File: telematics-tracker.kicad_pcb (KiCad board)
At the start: 4 copper layers, 82 x 62 mm, 216 parts, among them J1 WAFER-MX3.0-12PZZ, J2 B3B-XH-A, Q1 AM2390N-TP, Q10 MMBT3904, Q11 MMBT3904, Q12 MMBT3904, Q13 MMBT3906, Q14 MMBT3904, Q2 AM2390N-TP, Q3 AO3401A, Q4 MMBT3904, Q5 MMBT3904, Q6 MMBT3904, Q7 MMBT3904, Q8 MMBT3904, Q9 MMBT3904, U1 EC200UCNAA-N05-SGNSA, U2 AT32F403ACGT7, U3 QMI8658B, U4 SIT1051AT/3, U5 EG11752, U6 BQ25606RGER, U7 GD25Q64ESIGR, U8 TXB0104PWR, U9 ME6211C33M5G, X1 NANO-SIM, X2 MFF2-eSIM-pads, Y1 8MHz, Y2 32.768kHz

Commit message: hybrid v11 cycle 1: unconnected=150 errors=0
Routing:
- net 3V3: track 24.0 -> 54.1 mm
- net /modem_rf/VDD_EXT_1V8: track 86.2 -> 89.1 mm
- net 5V0: track 292.8 -> 294.7 mm, vias 22 -> 13
- net /mcu/BOOT0: track 2.42 -> 3.99 mm
- net /io/CAN_SPLIT: track 51.6 -> 53.1 mm
- net /mcu/VBAT_MCU: track 30.1 -> 31.5 mm
- net /modem_rf/Q12_B: track 120.4 -> 121.5 mm
- net /modem_rf/USIM_RST_M: track 77.6 -> 78.7 mm
- net /mcu/OSC32_IN: track 17.2 -> 18.3 mm
- net /mcu/I2C1_SDA: track 14.4 -> 15.1 mm
- net /mcu/I2C1_SCL: track 15.0 -> 15.7 mm
- net MODEM_PWRKEY: track 67.4 -> 68.0 mm

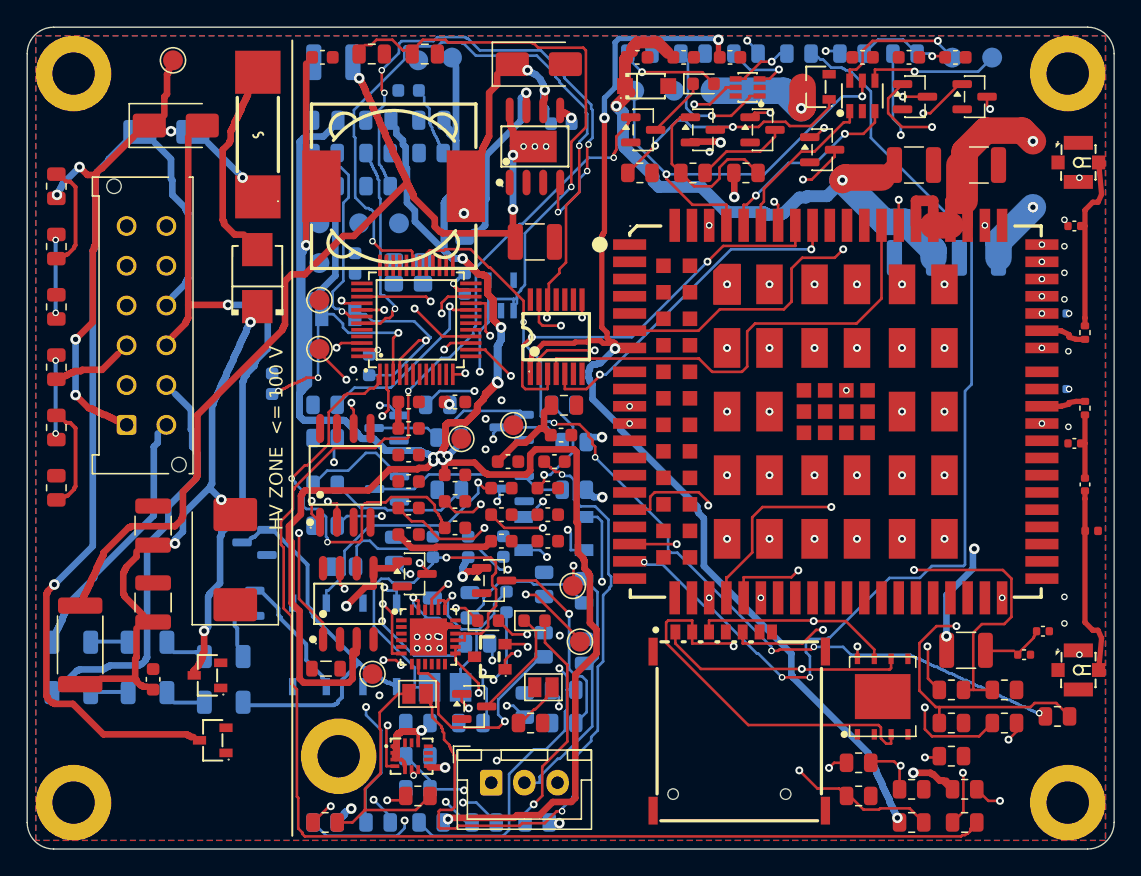
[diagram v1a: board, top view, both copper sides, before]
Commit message: hybrid v12 cycle 1: unconnected=110 errors=0
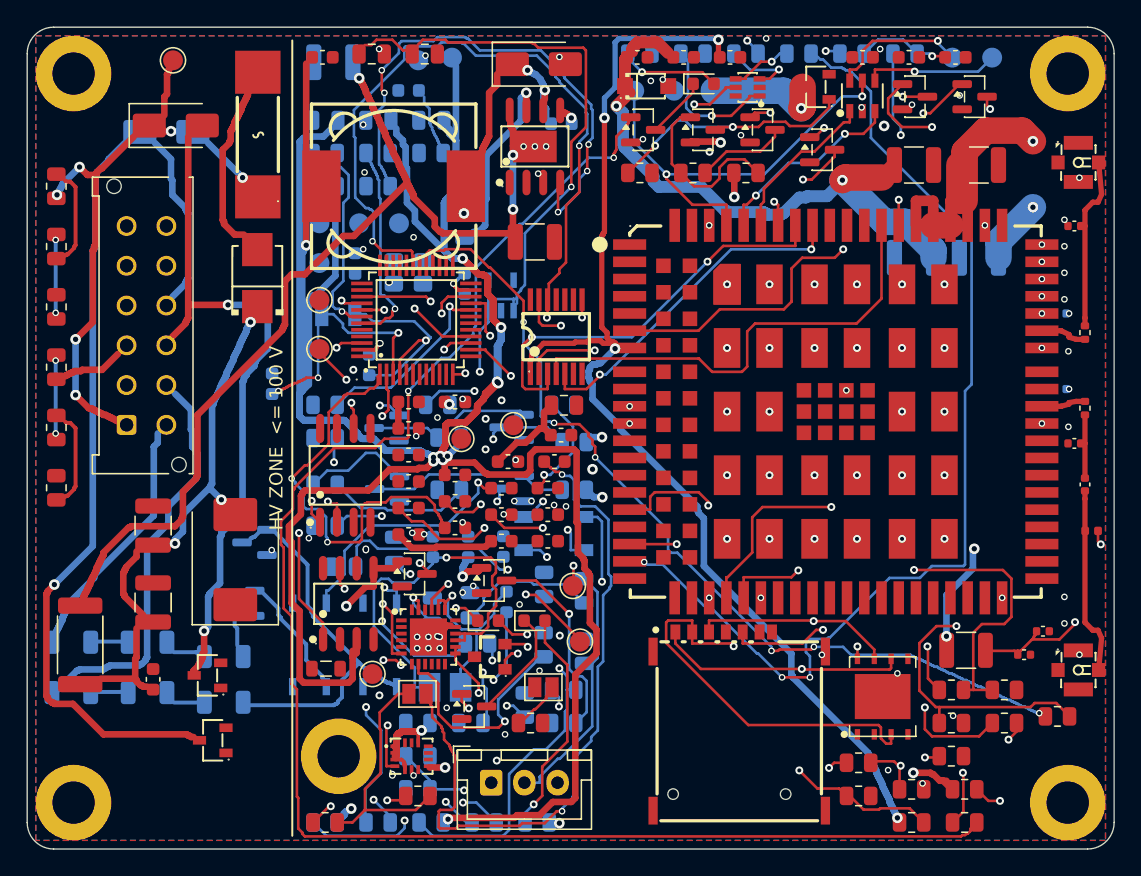
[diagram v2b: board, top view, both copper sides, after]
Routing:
- net /modem_rf/GNSS_BIAS: track 3.36 -> 16.6 mm, vias 0 -> 2
- net GND: track 3.62 -> 3.75 mm, vias 63 -> 112
- net 5V0: vias 13 -> 14
- net /modem_rf/VBAT_MODEM: vias 5 -> 6

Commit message: hybrid v12 cycle 2: unconnected=110 errors=0
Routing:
- net GND: vias 112 -> 110
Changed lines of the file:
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@@
 	(segment
 		(start 33.8996 45.4275)
-		(end 32.7628 45.4275)
+		(end 33.8996 47.2187)
 		(width 0.2)
 		(layer "B.Cu")
@@
 	(segment
 		(start 33.8996 45.4275)
-		(end 33.8996 47.2187)
+		(end 32.7628 45.4275)
 		(width 0.2)
 		(layer "B.Cu")
@@
 	(segment
 		(start 35.55 23.95)
-		(end 35.45 24.05)
+		(end 35.55 26.85)
 		(width 0.5)
 		(layer "B.Cu")
@@
 	(segment
 		(start 35.55 23.95)
-		(end 35.55 26.85)
+		(end 35.45 24.05)
 		(width 0.5)
 		(layer "B.Cu")
@@
 	(segment
 		(start 26.13 40.82)
-		(end 27.7625 40.82)
+		(end 26.13 42.2042)
 		(width 0.5)
 		(layer "F.Cu")
@@
 	(segment
 		(start 26.13 40.82)
-		(end 26.13 42.2042)
+		(end 27.7625 40.82)
 		(width 0.5)
 		(layer "F.Cu")
@@
 	(segment
 		(start 27.85 53.55)
-		(end 27.95 53.45)
+		(end 27.85 53.45)
 		(width 0.5)
 		(layer "F.Cu")
@@
 	(segment
 		(start 27.85 53.55)
-		(end 27.85 53.45)
+		(end 27.95 53.45)
 		(width 0.5)
 		(layer "F.Cu")
@@
 	(segment
 		(start 27.85 54.4)
-		(end 27.85 54.15)
+		(end 27.74 54.29)
 		(width 0.5)
 		(layer "F.Cu")
@@
 	(segment
 		(start 27.85 54.4)
-		(end 27.74 54.29)
+		(end 27.85 54.15)
 		(width 0.5)
 		(layer "F.Cu")
@@
 	(segment
 		(start 29.445 53.15)
-		(end 29.65 53.15)
+		(end 29.5 53.205)
 		(width 0.5)
 		(layer "F.Cu")
@@
 	(segment
 		(start 29.445 53.15)
-		(end 29.5 53.205)
+		(end 29.65 53.15)
 		(width 0.5)
 		(layer "F.Cu")
@@
 	(segment
 		(start 31.5 32.8)
-		(end 31.5 33.775)
+		(end 31.35 32.65)
 		(width 0.5)
 		(layer "F.Cu")
@@
 	(segment
 		(start 31.5 32.8)
-		(end 31.35 32.65)
+		(end 31.5 33.775)
 		(width 0.5)
 		(layer "F.Cu")
@@
 	(segment
 		(start 38.9927 30.2677)
-		(end 38.9927 29.0773)
+		(end 38.6729 30.2677)
 		(width 0.5)
 		(layer "F.Cu")
@@
 	(segment
 		(start 38.9927 30.2677)
-		(end 38.6729 30.2677)
+		(end 38.9927 29.0773)
 		(width 0.5)
 		(layer "F.Cu")
@@
 	(segment
 		(start 44.35 23.85)
-		(end 44.35 24.25)
-		(width 0.5)
+		(end 43.45 23.85)
+		(width 0.4)
 		(layer "F.Cu")
 		(net "/modem_rf/VDD_EXT_1V8")
@@
 	(segment
 		(start 44.35 23.85)
-		(end 43.45 23.85)
-		(width 0.4)
+		(end 44.35 24.25)
+		(width 0.5)
 		(layer "F.Cu")
 		(net "/modem_rf/VDD_EXT_1V8")
@@
 	)
 	(segment
-		(start 72.75 47.05)
-		(end 72.3325 47.05)
-		(width 0.2)
-		(layer "F.Cu")
-		(net "/modem_rf/GNSS_BIAS")
-	)
-	(segment
 		(start 72.8125 49.995)
 		(end 71.3739 49.995)
@@
 	)
 	(segment
-		(start 74.45 47.05)
-		(end 74.73 47.05)
-		(width 0.2)
-		(layer "F.Cu")
-		(net "/modem_rf/GNSS_BIAS")
-	)
-	(segment
-		(start 74.45 47.05)
-		(end 72.75 47.05)
-		(width 0.2)
-		(layer "F.Cu")
-		(net "/modem_rf/GNSS_BIAS")
-	)
-	(segment
 		(start 74.6375 53.1394)
 		(end 74.6375 52.495)
@@
 	)
 	(segment
+		(start 74.73 47.05)
+		(end 72.3325 47.05)
+		(width 0.2)
+		(layer "F.Cu")
+		(net "/modem_rf/GNSS_BIAS")
+	)
+	(segment
 		(start 74.95 47.05)
 		(end 75.8117 46.1883)
@@
 	(segment
 		(start 75.95 45.95)
-		(end 76.05 45.85)
+		(end 76.15 45.75)
 		(width 0.2)
 		(layer "F.Cu")
@@
 	)
 	(segment
-		(start 76.05 45.85)
-		(end 76.15 45.75)
-		(width 0.2)
-		(layer "F.Cu")
-		(net "/modem_rf/GNSS_BIAS")
-	)
-	(segment
 		(start 76.15 45.75)
 		(end 76.15 45.57)
@@
 	(segment
 		(start 26.5757 50.408)
-		(end 25.6935 49.5258)
+		(end 26.5757 52.9057)
 		(width 0.2)
 		(layer "In2.Cu")
@@
 	(segment
 		(start 26.5757 50.408)
-		(end 26.5757 52.9057)
+		(end 25.6935 49.5258)
 		(width 0.2)
 		(layer "In2.Cu")
@@
 	(segment
 		(start 50.8504 9.3985)
-		(end 50.7221 9.5268)
+		(end 51.4768 9.3985)
 		(width 0.2)
 		(layer "In2.Cu")
@@
 	(segment
 		(start 50.8504 9.3985)
-		(end 51.4768 9.3985)
+		(end 50.7221 9.5268)
 		(width 0.2)
 		(layer "In2.Cu")
@@
 	(segment
 		(start 68.6767 53.2666)
-		(end 73.5529 53.2666)
+		(end 68.6767 54.1421)
 		(width 0.2)
 		(layer "In2.Cu")
@@
 	(segment
 		(start 68.6767 53.2666)
-		(end 68.6767 54.1421)
+		(end 73.5529 53.2666)
 		(width 0.2)
 		(layer "In2.Cu")
@@
 	)
 	(via
-		(at 29.95 38.25)
-		(size 0.5)
-		(drill 0.3)
-		(layers "F.Cu" "B.Cu")
-		(net "GND")
-	)
-	(via
 		(at 30.05 2.15)
 		(size 0.5)
@@
 	)
 	(via
-		(at 38.05 35.75)
-		(size 0.5)
-		(drill 0.3)
-		(layers "F.Cu" "B.Cu")
-		(net "GND")
-	)
-	(via
 		(at 38.0763 23.3884)
 		(size 0.6)
@@
 	)
 	(via
-		(at 47.05 4.05)
+		(at 47.15 3.95)
 		(size 0.5)
 		(drill 0.3)
@@
 	)
 	(via
-		(at 47.95 3.95)
+		(at 48.05 4.05)
 		(size 0.5)
 		(drill 0.3)
